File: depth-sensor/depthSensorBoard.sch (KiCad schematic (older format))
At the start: 12 parts, among them P1 CONN_01X05, P3 CONN_01X04, P4 CONN_01X04, P5 CONN_01X04, P6 CONN_01X04, Q2 Q_NJFET_GSD, U1 LM3480-3.3, U2 TCA9545A

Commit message: Changed part number for capacitors
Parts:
- C1, C2, C3, C4: part number 490-5881-2-ND -> 311-1343-1-ND
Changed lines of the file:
@@
 F 2 "Capacitors_SMD:C_0603" H 3438 1350 50  0001 C CNN
 F 3 "" H 3400 1500 50  0000 C CNN
-F 4 "490-5881-2-ND" H 3400 1500 60  0001 C CNN "part number"
+F 4 "311-1343-1-ND" H 3400 1500 60  0001 C CNN "part number"
 	1    3400 1500
 	1    0    0    -1
@@
 F 2 "Capacitors_SMD:C_0603" H 4438 1350 50  0001 C CNN
 F 3 "" H 4400 1500 50  0000 C CNN
-F 4 "490-5881-2-ND" H 4400 1500 60  0001 C CNN "part number"
+F 4 "311-1343-1-ND" H 4400 1500 60  0001 C CNN "part number"
 	1    4400 1500
 	1    0    0    -1
@@
 F 2 "Capacitors_SMD:C_0603" H 638 2900 50  0001 C CNN
 F 3 "" H 600 3050 50  0000 C CNN
-F 4 "490-5881-2-ND" H 600 3050 60  0001 C CNN "part number"
+F 4 "311-1343-1-ND" H 600 3050 60  0001 C CNN "part number"
 	1    600  3050
 	1    0    0    -1
@@
 F 2 "Capacitors_SMD:C_0603" H 988 2900 50  0001 C CNN
 F 3 "" H 950 3050 50  0000 C CNN
-F 4 "490-5881-2-ND" H 950 3050 60  0001 C CNN "part number"
+F 4 "311-1343-1-ND" H 950 3050 60  0001 C CNN "part number"
 	1    950  3050
 	1    0    0    -1

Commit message: Added connector part numbers and footprints
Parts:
- P1: part number (none) -> CP-2350-ND
- P3, P4, P5, P6: footprint Pin_Headers:Pin_Header_Straight_1x04 -> robosub_footprints:cui-4-board-f; part number (none) -> CP-2340-ND
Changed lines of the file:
@@
 F 0 "P3" H 8250 2350 50  0000 C CNN
 F 1 "CONN_01X04" V 8350 2100 50  0000 C CNN
-F 2 "Pin_Headers:Pin_Header_Straight_1x04" H 8250 2100 50  0001 C CNN
+F 2 "robosub_footprints:cui-4-board-f" H 8250 2100 50  0001 C CNN
 F 3 "" H 8250 2100 50  0000 C CNN
+F 4 "CP-2340-ND" H 8250 2100 60  0001 C CNN "part number"
 	1    8250 2100
 	1    0    0    -1
@@
 F 0 "P4" H 8250 3450 50  0000 C CNN
 F 1 "CONN_01X04" V 8350 3200 50  0000 C CNN
-F 2 "Pin_Headers:Pin_Header_Straight_1x04" H 8250 3200 50  0001 C CNN
+F 2 "robosub_footprints:cui-4-board-f" H 8250 3200 50  0001 C CNN
 F 3 "" H 8250 3200 50  0000 C CNN
+F 4 "CP-2340-ND" H 8250 3200 60  0001 C CNN "part number"
 	1    8250 3200
 	1    0    0    -1
@@
 F 0 "P5" H 8250 4600 50  0000 C CNN
 F 1 "CONN_01X04" V 8350 4350 50  0000 C CNN
-F 2 "Pin_Headers:Pin_Header_Straight_1x04" H 8250 4350 50  0001 C CNN
+F 2 "robosub_footprints:cui-4-board-f" H 8250 4350 50  0001 C CNN
 F 3 "" H 8250 4350 50  0000 C CNN
+F 4 "CP-2340-ND" H 8250 4350 60  0001 C CNN "part number"
 	1    8250 4350
 	1    0    0    -1
@@
 F 0 "P6" H 8250 5600 50  0000 C CNN
 F 1 "CONN_01X04" V 8350 5350 50  0000 C CNN
-F 2 "Pin_Headers:Pin_Header_Straight_1x04" H 8250 5350 50  0001 C CNN
+F 2 "robosub_footprints:cui-4-board-f" H 8250 5350 50  0001 C CNN
 F 3 "" H 8250 5350 50  0000 C CNN
+F 4 "CP-2340-ND" H 8250 5350 60  0001 C CNN "part number"
 	1    8250 5350
 	1    0    0    -1
@@
 F 2 "robosub_footprints:cui-5-board-f" H 1550 1550 50  0001 C CNN
 F 3 "" H 1550 1550 50  0000 C CNN
+F 4 "CP-2350-ND" H 1550 1550 60  0001 C CNN "part number"
 	1    1550 1550
 	-1   0    0    -1
@@
 $EndComp
 $Comp
-L GND #PWR?
+L GND #PWR016
 U 1 1 581C6BD6
 P 1300 3700
-F 0 "#PWR?" H 1300 3450 50  0001 C CNN
+F 0 "#PWR016" H 1300 3450 50  0001 C CNN
 F 1 "GND" H 1300 3550 50  0000 C CNN
 F 2 "" H 1300 3700 50  0000 C CNN

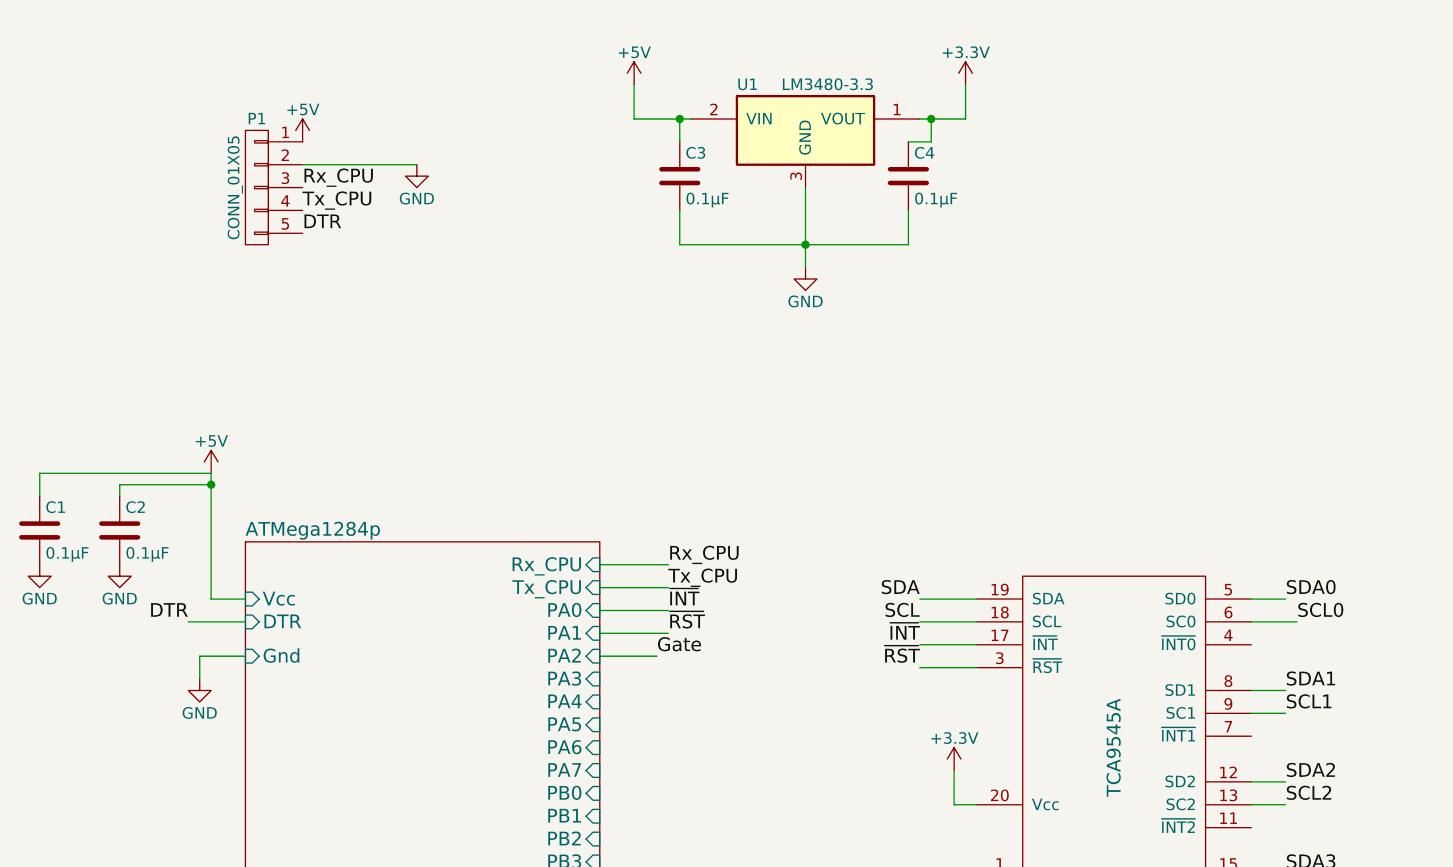
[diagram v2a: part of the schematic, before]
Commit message: Added AP2112 to library and LEDs to schematic
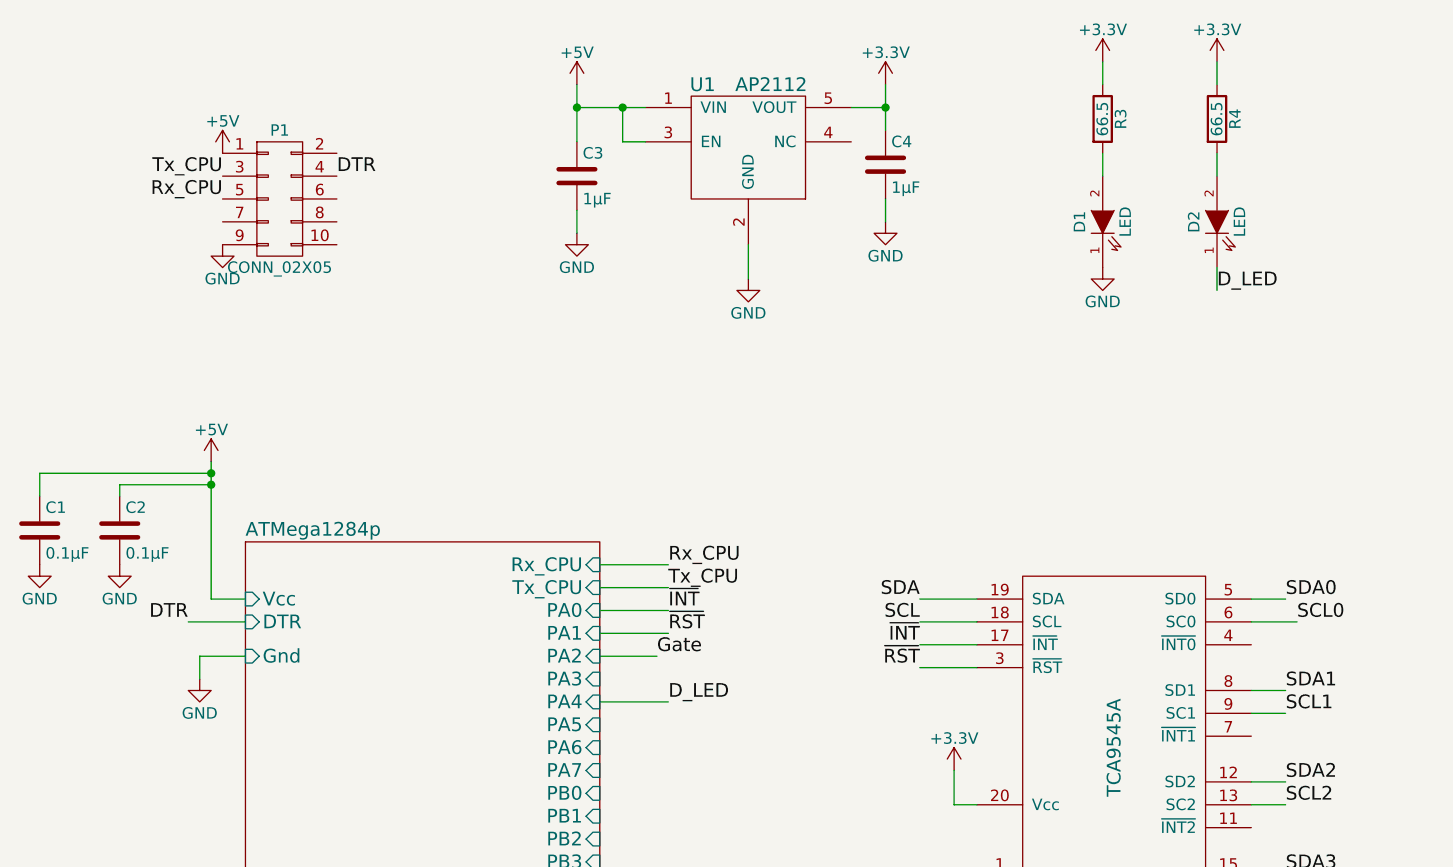
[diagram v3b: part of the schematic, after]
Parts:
- removed P1: CONN_01X05, robosub_footprints:cui-5-board-f, symbol CONN_01X05
- removed U1: LM3480-3.3, TO_SOT_Packages_SMD:SOT-23, symbol LM3480-3.3
- added D1, D2: LED, LEDs:LED_0603, symbol LED
- added P1: CONN_02X05, symbol CONN_02X05
- added R3, R4: 66.5, Resistors_SMD:R_0603, symbol R
- added U1: AP2112, TO_SOT_Packages_SMD:SOT-23-5, symbol AP2112
- C3, C4: value 0.1μF -> 1µF; part number 311-1343-1-ND -> 311-1372-1-ND
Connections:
- net +3V3: now also R3.1, R4.1, U1.5 (VOUT)
- net +5V: now also P1.1 (P1), U1.1 (VIN), U1.3 (EN)
- net DTR: now also P1.4 (P4)
- net GND: now also D1.1 (K), P1.9 (P9), U1.2 (GND)
- net Rx_CPU: now also P1.5 (P5)
- net Tx_CPU: now also P1.3 (P3)
- new net: D2.2 (A), R4.2
- new net: D1.2 (A), R3.2
- new net D_LED: D2.1 (K)

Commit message: Added RJ10 Jack footprint
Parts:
- P3, P4, P5, P6: footprint robosub_footprints:cui-4-board-f -> robosub_footprints:RJ10-JACK; part number CP-2340-ND -> AE10381-ND
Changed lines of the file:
@@
 F 0 "P3" H 8250 2350 50  0000 C CNN
 F 1 "CONN_01X04" V 8350 2100 50  0000 C CNN
-F 2 "robosub_footprints:cui-4-board-f" H 8250 2100 50  0001 C CNN
+F 2 "robosub_footprints:RJ10-JACK" H 8250 2100 50  0001 C CNN
 F 3 "" H 8250 2100 50  0000 C CNN
-F 4 "CP-2340-ND" H 8250 2100 60  0001 C CNN "part number"
+F 4 "AE10381-ND" H 8250 2100 60  0001 C CNN "part number"
 	1    8250 2100
 	1    0    0    -1
@@
 F 0 "P4" H 8250 3450 50  0000 C CNN
 F 1 "CONN_01X04" V 8350 3200 50  0000 C CNN
-F 2 "robosub_footprints:cui-4-board-f" H 8250 3200 50  0001 C CNN
+F 2 "robosub_footprints:RJ10-JACK" H 8250 3200 50  0001 C CNN
 F 3 "" H 8250 3200 50  0000 C CNN
-F 4 "CP-2340-ND" H 8250 3200 60  0001 C CNN "part number"
+F 4 "AE10381-ND" H 8250 3200 60  0001 C CNN "part number"
 	1    8250 3200
 	1    0    0    -1
@@
 F 0 "P5" H 8250 4600 50  0000 C CNN
 F 1 "CONN_01X04" V 8350 4350 50  0000 C CNN
-F 2 "robosub_footprints:cui-4-board-f" H 8250 4350 50  0001 C CNN
+F 2 "robosub_footprints:RJ10-JACK" H 8250 4350 50  0001 C CNN
 F 3 "" H 8250 4350 50  0000 C CNN
-F 4 "CP-2340-ND" H 8250 4350 60  0001 C CNN "part number"
+F 4 "AE10381-ND" H 8250 4350 60  0001 C CNN "part number"
 	1    8250 4350
 	1    0    0    -1
@@
 F 0 "P6" H 8250 5600 50  0000 C CNN
 F 1 "CONN_01X04" V 8350 5350 50  0000 C CNN
-F 2 "robosub_footprints:cui-4-board-f" H 8250 5350 50  0001 C CNN
+F 2 "robosub_footprints:RJ10-JACK" H 8250 5350 50  0001 C CNN
 F 3 "" H 8250 5350 50  0000 C CNN
-F 4 "CP-2340-ND" H 8250 5350 60  0001 C CNN "part number"
+F 4 "AE10381-ND" H 8250 5350 60  0001 C CNN "part number"
 	1    8250 5350
 	1    0    0    -1
@@
 SCL3
 $Comp
-L GND #PWR13
+L GND #PWR01
 U 1 1 57E8E35F
 P 4600 4800
-F 0 "#PWR13" H 4600 4550 50  0001 C CNN
+F 0 "#PWR01" H 4600 4550 50  0001 C CNN
 F 1 "GND" H 4600 4650 50  0000 C CNN
 F 2 "" H 4600 4800 50  0000 C CNN
@@
 $EndComp
 $Comp
-L +3.3V #PWR12
+L +3.3V #PWR02
 U 1 1 57EC819B
 P 4600 4100
-F 0 "#PWR12" H 4600 3950 50  0001 C CNN
+F 0 "#PWR02" H 4600 3950 50  0001 C CNN
 F 1 "+3.3V" H 4600 4240 50  0000 C CNN
 F 2 "" H 4600 4100 50  0000 C CNN
@@
 SCL0
 $Comp
-L GND #PWR17
+L GND #PWR03
 U 1 1 57EE7883
 P 6700 6100
-F 0 "#PWR17" H 6700 5850 50  0001 C CNN
+F 0 "#PWR03" H 6700 5850 50  0001 C CNN
 F 1 "GND" H 6700 5950 50  0000 C CNN
 F 2 "" H 6700 6100 50  0000 C CNN
@@
 $EndComp
 $Comp
-L +3.3V #PWR18
+L +3.3V #PWR04
 U 1 1 57EE7C6C
 P 8050 1950
-F 0 "#PWR18" H 8050 1800 50  0001 C CNN
+F 0 "#PWR04" H 8050 1800 50  0001 C CNN
 F 1 "+3.3V" H 8050 2090 50  0000 C CNN
 F 2 "" H 8050 1950 50  0000 C CNN
@@
 $EndComp
 $Comp
-L +3.3V #PWR19
+L +3.3V #PWR05
 U 1 1 57EE7CA0
 P 8050 3050
-F 0 "#PWR19" H 8050 2900 50  0001 C CNN
+F 0 "#PWR05" H 8050 2900 50  0001 C CNN
 F 1 "+3.3V" H 8050 3190 50  0000 C CNN
 F 2 "" H 8050 3050 50  0000 C CNN
@@
 $EndComp
 $Comp
-L +3.3V #PWR20
+L +3.3V #PWR06
 U 1 1 57EE7DD4
 P 8050 4200
-F 0 "#PWR20" H 8050 4050 50  0001 C CNN
+F 0 "#PWR06" H 8050 4050 50  0001 C CNN
 F 1 "+3.3V" H 8050 4340 50  0000 C CNN
 F 2 "" H 8050 4200 50  0000 C CNN
@@
 $EndComp
 $Comp
-L +3.3V #PWR21
+L +3.3V #PWR07
 U 1 1 57EE7E08
 P 8050 5200
-F 0 "#PWR21" H 8050 5050 50  0001 C CNN
+F 0 "#PWR07" H 8050 5050 50  0001 C CNN
 F 1 "+3.3V" H 8050 5340 50  0000 C CNN
 F 2 "" H 8050 5200 50  0000 C CNN
@@
 ~RST
 $Comp
-L +5V #PWR4
+L +5V #PWR08
 U 1 1 580F6AF3
 P 1350 2750
-F 0 "#PWR4" H 1350 2600 50  0001 C CNN
+F 0 "#PWR08" H 1350 2600 50  0001 C CNN
 F 1 "+5V" H 1350 2890 50  0000 C CNN
 F 2 "" H 1350 2750 50  0000 C CNN
@@
 $EndComp
 $Comp
-L GND #PWR1
+L GND #PWR09
 U 1 1 580F9091
 P 600 3200
-F 0 "#PWR1" H 600 2950 50  0001 C CNN
+F 0 "#PWR09" H 600 2950 50  0001 C CNN
 F 1 "GND" H 600 3050 50  0000 C CNN
 F 2 "" H 600 3200 50  0000 C CNN
@@
 $EndComp
 $Comp
-L GND #PWR2
+L GND #PWR010
 U 1 1 580F917D
 P 950 3200
-F 0 "#PWR2" H 950 2950 50  0001 C CNN
+F 0 "#PWR010" H 950 2950 50  0001 C CNN
 F 1 "GND" H 950 3050 50  0000 C CNN
 F 2 "" H 950 3200 50  0000 C CNN
@@
 $EndComp
 $Comp
-L GND #PWR3
+L GND #PWR011
 U 1 1 581C6BD6
 P 1300 3700
-F 0 "#PWR3" H 1300 3450 50  0001 C CNN
+F 0 "#PWR011" H 1300 3450 50  0001 C CNN
 F 1 "GND" H 1300 3550 50  0000 C CNN
 F 2 "" H 1300 3700 50  0000 C CNN
@@
 $EndComp
 $Comp
-L +5V #PWR5
+L +5V #PWR012
 U 1 1 58253494
 P 1400 1400
-F 0 "#PWR5" H 1400 1250 50  0001 C CNN
+F 0 "#PWR012" H 1400 1250 50  0001 C CNN
 F 1 "+5V" H 1400 1540 50  0000 C CNN
 F 2 "" H 1400 1400 50  0000 C CNN
@@
 $EndComp
 $Comp
-L GND #PWR6
+L GND #PWR013
 U 1 1 58253582
 P 1400 1800
-F 0 "#PWR6" H 1400 1550 50  0001 C CNN
+F 0 "#PWR013" H 1400 1550 50  0001 C CNN
 F 1 "GND" H 1400 1650 50  0000 C CNN
 F 2 "" H 1400 1800 50  0000 C CNN
@@
 DTR
 $Comp
-L +5V #PWR7
+L +5V #PWR014
 U 1 1 58254C2A
 P 2950 1100
-F 0 "#PWR7" H 2950 950 50  0001 C CNN
+F 0 "#PWR014" H 2950 950 50  0001 C CNN
 F 1 "+5V" H 2950 1240 50  0000 C CNN
 F 2 "" H 2950 1100 50  0000 C CNN
@@
 $EndComp
 $Comp
-L +3.3V #PWR10
+L +3.3V #PWR015
 U 1 1 58257735
 P 4300 1100
-F 0 "#PWR10" H 4300 950 50  0001 C CNN
+F 0 "#PWR015" H 4300 950 50  0001 C CNN
 F 1 "+3.3V" H 4300 1240 50  0000 C CNN
 F 2 "" H 4300 1100 50  0000 C CNN
@@
 $EndComp
 $Comp
-L +3.3V #PWR14
+L +3.3V #PWR016
 U 1 1 5825D2CB
 P 5250 1000
-F 0 "#PWR14" H 5250 850 50  0001 C CNN
+F 0 "#PWR016" H 5250 850 50  0001 C CNN
 F 1 "+3.3V" H 5250 1140 50  0000 C CNN
 F 2 "" H 5250 1000 50  0000 C CNN
@@
 $EndComp
 $Comp
-L GND #PWR15
+L GND #PWR017
 U 1 1 5825D2D8
 P 5250 1900
-F 0 "#PWR15" H 5250 1650 50  0001 C CNN
+F 0 "#PWR017" H 5250 1650 50  0001 C CNN
 F 1 "GND" H 5250 1750 50  0000 C CNN
 F 2 "" H 5250 1900 50  0000 C CNN
@@
 D_LED
 $Comp
-L +3.3V #PWR16
+L +3.3V #PWR018
 U 1 1 5825F861
 P 5750 1000
-F 0 "#PWR16" H 5750 850 50  0001 C CNN
+F 0 "#PWR018" H 5750 850 50  0001 C CNN
 F 1 "+3.3V" H 5750 1140 50  0000 C CNN
 F 2 "" H 5750 1000 50  0000 C CNN
@@
 $EndComp
 $Comp
-L GND #PWR8
+L GND #PWR019
 U 1 1 5826A6AD
 P 2950 1750
-F 0 "#PWR8" H 2950 1500 50  0001 C CNN
+F 0 "#PWR019" H 2950 1500 50  0001 C CNN
 F 1 "GND" H 2950 1600 50  0000 C CNN
 F 2 "" H 2950 1750 50  0000 C CNN
@@
 $EndComp
 $Comp
-L GND #PWR11
+L GND #PWR020
 U 1 1 5826AB64
 P 4300 1700
-F 0 "#PWR11" H 4300 1450 50  0001 C CNN
+F 0 "#PWR020" H 4300 1450 50  0001 C CNN
 F 1 "GND" H 4300 1550 50  0000 C CNN
 F 2 "" H 4300 1700 50  0000 C CNN
@@
 $EndComp
 $Comp
-L GND #PWR9
+L GND #PWR021
 U 1 1 5826B4FA
 P 3700 1950
-F 0 "#PWR9" H 3700 1700 50  0001 C CNN
+F 0 "#PWR021" H 3700 1700 50  0001 C CNN
 F 1 "GND" H 3700 1800 50  0000 C CNN
 F 2 "" H 3700 1950 50  0000 C CNN

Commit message: Schematic finished and Attempted PCB layout
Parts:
- P1: footprint (none) -> robosub_footprints:DF40C-10DP-Header; part number (none) -> H11616CT-ND
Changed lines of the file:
@@
 SCL3
 $Comp
-L GND #PWR01
+L GND #PWR13
 U 1 1 57E8E35F
 P 4600 4800
-F 0 "#PWR01" H 4600 4550 50  0001 C CNN
+F 0 "#PWR13" H 4600 4550 50  0001 C CNN
 F 1 "GND" H 4600 4650 50  0000 C CNN
 F 2 "" H 4600 4800 50  0000 C CNN
@@
 $EndComp
 $Comp
-L +3.3V #PWR02
+L +3.3V #PWR12
 U 1 1 57EC819B
 P 4600 4100
-F 0 "#PWR02" H 4600 3950 50  0001 C CNN
+F 0 "#PWR12" H 4600 3950 50  0001 C CNN
 F 1 "+3.3V" H 4600 4240 50  0000 C CNN
 F 2 "" H 4600 4100 50  0000 C CNN
@@
 SCL0
 $Comp
-L GND #PWR03
+L GND #PWR17
 U 1 1 57EE7883
 P 6700 6100
-F 0 "#PWR03" H 6700 5850 50  0001 C CNN
+F 0 "#PWR17" H 6700 5850 50  0001 C CNN
 F 1 "GND" H 6700 5950 50  0000 C CNN
 F 2 "" H 6700 6100 50  0000 C CNN
@@
 $EndComp
 $Comp
-L +3.3V #PWR04
+L +3.3V #PWR18
 U 1 1 57EE7C6C
 P 8050 1950
-F 0 "#PWR04" H 8050 1800 50  0001 C CNN
+F 0 "#PWR18" H 8050 1800 50  0001 C CNN
 F 1 "+3.3V" H 8050 2090 50  0000 C CNN
 F 2 "" H 8050 1950 50  0000 C CNN
@@
 $EndComp
 $Comp
-L +3.3V #PWR05
+L +3.3V #PWR19
 U 1 1 57EE7CA0
 P 8050 3050
-F 0 "#PWR05" H 8050 2900 50  0001 C CNN
+F 0 "#PWR19" H 8050 2900 50  0001 C CNN
 F 1 "+3.3V" H 8050 3190 50  0000 C CNN
 F 2 "" H 8050 3050 50  0000 C CNN
@@
 $EndComp
 $Comp
-L +3.3V #PWR06
+L +3.3V #PWR20
 U 1 1 57EE7DD4
 P 8050 4200
-F 0 "#PWR06" H 8050 4050 50  0001 C CNN
+F 0 "#PWR20" H 8050 4050 50  0001 C CNN
 F 1 "+3.3V" H 8050 4340 50  0000 C CNN
 F 2 "" H 8050 4200 50  0000 C CNN
@@
 $EndComp
 $Comp
-L +3.3V #PWR07
+L +3.3V #PWR21
 U 1 1 57EE7E08
 P 8050 5200
-F 0 "#PWR07" H 8050 5050 50  0001 C CNN
+F 0 "#PWR21" H 8050 5050 50  0001 C CNN
 F 1 "+3.3V" H 8050 5340 50  0000 C CNN
 F 2 "" H 8050 5200 50  0000 C CNN
@@
 ~RST
 $Comp
-L +5V #PWR08
+L +5V #PWR4
 U 1 1 580F6AF3
 P 1350 2750
-F 0 "#PWR08" H 1350 2600 50  0001 C CNN
+F 0 "#PWR4" H 1350 2600 50  0001 C CNN
 F 1 "+5V" H 1350 2890 50  0000 C CNN
 F 2 "" H 1350 2750 50  0000 C CNN
@@
 $EndComp
 $Comp
-L GND #PWR09
+L GND #PWR1
 U 1 1 580F9091
 P 600 3200
-F 0 "#PWR09" H 600 2950 50  0001 C CNN
+F 0 "#PWR1" H 600 2950 50  0001 C CNN
 F 1 "GND" H 600 3050 50  0000 C CNN
 F 2 "" H 600 3200 50  0000 C CNN
@@
 $EndComp
 $Comp
-L GND #PWR010
+L GND #PWR2
 U 1 1 580F917D
 P 950 3200
-F 0 "#PWR010" H 950 2950 50  0001 C CNN
+F 0 "#PWR2" H 950 2950 50  0001 C CNN
 F 1 "GND" H 950 3050 50  0000 C CNN
 F 2 "" H 950 3200 50  0000 C CNN
@@
 $EndComp
 $Comp
-L GND #PWR011
+L GND #PWR3
 U 1 1 581C6BD6
 P 1300 3700
-F 0 "#PWR011" H 1300 3450 50  0001 C CNN
+F 0 "#PWR3" H 1300 3450 50  0001 C CNN
 F 1 "GND" H 1300 3550 50  0000 C CNN
 F 2 "" H 1300 3700 50  0000 C CNN
@@
 F 0 "P1" H 1650 1900 50  0000 C CNN
 F 1 "CONN_02X05" H 1650 1300 50  0000 C CNN
-F 2 "" H 1650 400 50  0001 C CNN
+F 2 "robosub_footprints:DF40C-10DP-Header" H 1650 400 50  0001 C CNN
 F 3 "" H 1650 400 50  0000 C CNN
+F 4 "H11616CT-ND" H 1650 1600 60  0001 C CNN "part number"
 	1    1650 1600
 	1    0    0    -1
 $EndComp
 $Comp
-L +5V #PWR012
+L +5V #PWR5
 U 1 1 58253494
 P 1400 1400
-F 0 "#PWR012" H 1400 1250 50  0001 C CNN
+F 0 "#PWR5" H 1400 1250 50  0001 C CNN
 F 1 "+5V" H 1400 1540 50  0000 C CNN
 F 2 "" H 1400 1400 50  0000 C CNN
@@
 $EndComp
 $Comp
-L GND #PWR013
+L GND #PWR6
 U 1 1 58253582
 P 1400 1800
-F 0 "#PWR013" H 1400 1550 50  0001 C CNN
+F 0 "#PWR6" H 1400 1550 50  0001 C CNN
 F 1 "GND" H 1400 1650 50  0000 C CNN
 F 2 "" H 1400 1800 50  0000 C CNN
@@
 DTR
 $Comp
-L +5V #PWR014
+L +5V #PWR7
 U 1 1 58254C2A
 P 2950 1100
-F 0 "#PWR014" H 2950 950 50  0001 C CNN
+F 0 "#PWR7" H 2950 950 50  0001 C CNN
 F 1 "+5V" H 2950 1240 50  0000 C CNN
 F 2 "" H 2950 1100 50  0000 C CNN
@@
 $EndComp
 $Comp
-L +3.3V #PWR015
+L +3.3V #PWR10
 U 1 1 58257735
 P 4300 1100
-F 0 "#PWR015" H 4300 950 50  0001 C CNN
+F 0 "#PWR10" H 4300 950 50  0001 C CNN
 F 1 "+3.3V" H 4300 1240 50  0000 C CNN
 F 2 "" H 4300 1100 50  0000 C CNN
@@
 $EndComp
 $Comp
-L +3.3V #PWR016
+L +3.3V #PWR14
 U 1 1 5825D2CB
 P 5250 1000
-F 0 "#PWR016" H 5250 850 50  0001 C CNN
+F 0 "#PWR14" H 5250 850 50  0001 C CNN
 F 1 "+3.3V" H 5250 1140 50  0000 C CNN
 F 2 "" H 5250 1000 50  0000 C CNN
@@
 $EndComp
 $Comp
-L GND #PWR017
+L GND #PWR15
 U 1 1 5825D2D8
 P 5250 1900
-F 0 "#PWR017" H 5250 1650 50  0001 C CNN
+F 0 "#PWR15" H 5250 1650 50  0001 C CNN
 F 1 "GND" H 5250 1750 50  0000 C CNN
 F 2 "" H 5250 1900 50  0000 C CNN
@@
 D_LED
 $Comp
-L +3.3V #PWR018
+L +3.3V #PWR16
 U 1 1 5825F861
 P 5750 1000
-F 0 "#PWR018" H 5750 850 50  0001 C CNN
+F 0 "#PWR16" H 5750 850 50  0001 C CNN
 F 1 "+3.3V" H 5750 1140 50  0000 C CNN
 F 2 "" H 5750 1000 50  0000 C CNN
@@
 $EndComp
 $Comp
-L GND #PWR019
+L GND #PWR8
 U 1 1 5826A6AD
 P 2950 1750
-F 0 "#PWR019" H 2950 1500 50  0001 C CNN
+F 0 "#PWR8" H 2950 1500 50  0001 C CNN
 F 1 "GND" H 2950 1600 50  0000 C CNN
 F 2 "" H 2950 1750 50  0000 C CNN
@@
 $EndComp
 $Comp
-L GND #PWR020
+L GND #PWR11
 U 1 1 5826AB64
 P 4300 1700
-F 0 "#PWR020" H 4300 1450 50  0001 C CNN
+F 0 "#PWR11" H 4300 1450 50  0001 C CNN
 F 1 "GND" H 4300 1550 50  0000 C CNN
 F 2 "" H 4300 1700 50  0000 C CNN
@@
 $EndComp
 $Comp
-L GND #PWR021
+L GND #PWR9
 U 1 1 5826B4FA
 P 3700 1950
-F 0 "#PWR021" H 3700 1700 50  0001 C CNN
+F 0 "#PWR9" H 3700 1700 50  0001 C CNN
 F 1 "GND" H 3700 1800 50  0000 C CNN
 F 2 "" H 3700 1950 50  0000 C CNN
